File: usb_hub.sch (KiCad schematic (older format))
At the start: 26 parts, among them U3 USB2514B_Bi, Y1 24MHz

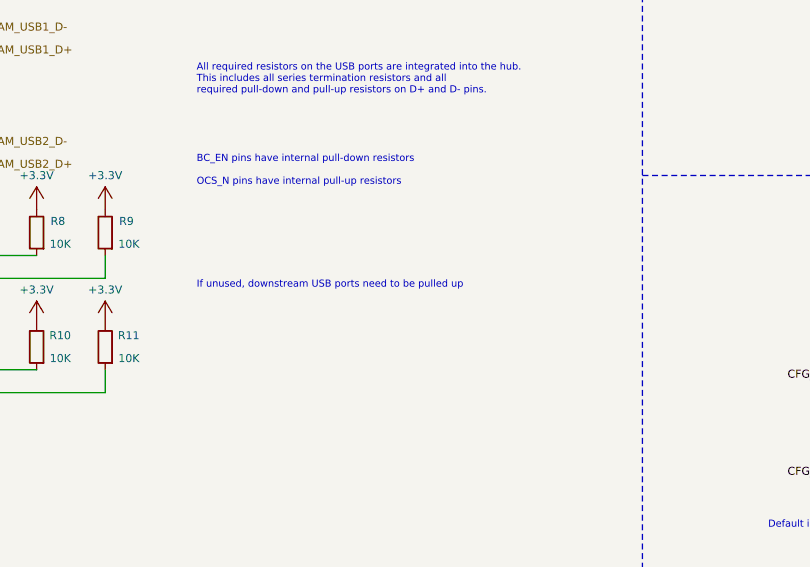
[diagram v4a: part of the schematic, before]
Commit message: Add fiducials, finish routing
Signed-off-by: Tomislav Milkovic <tomislav.milkovic95@gmail.com>
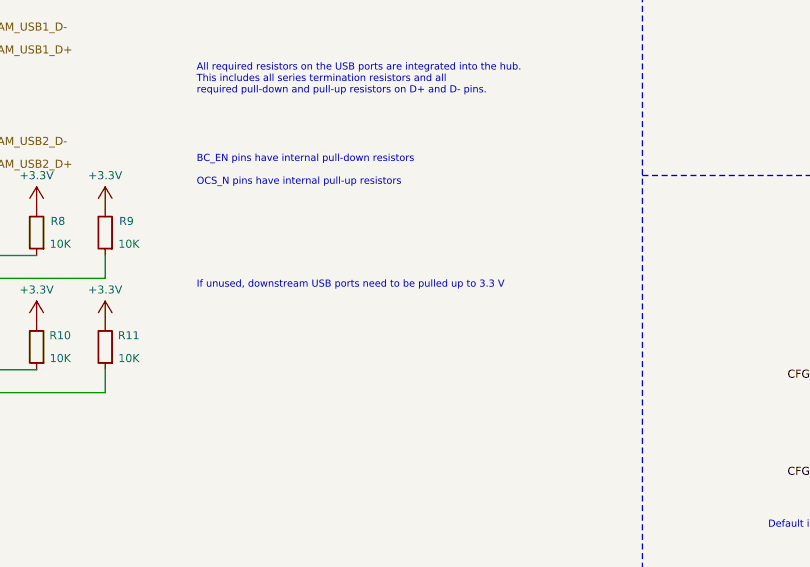
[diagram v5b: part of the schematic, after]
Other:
- note added: "If unused, downstream USB ports need to be pulled up to 3.3 V"
- note removed: "If unused, downstream USB ports need to be pulled up"
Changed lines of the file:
@@
 OCS_N pins have internal pull-up resistors
 Text Notes 5500 3350 0    31   ~ 0
-If unused, downstream USB ports need to be pulled up
+If unused, downstream USB ports need to be pulled up to 3.3 V
 Wire Wire Line
 	8950 1550 8950 1800
